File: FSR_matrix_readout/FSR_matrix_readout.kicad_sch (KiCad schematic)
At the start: 6 parts, among them U1 NCD98010XMXTAG, U2 NCD98010XMXTAG, U4 TPW4051-QF4R, U5 TPW4051-QF4R

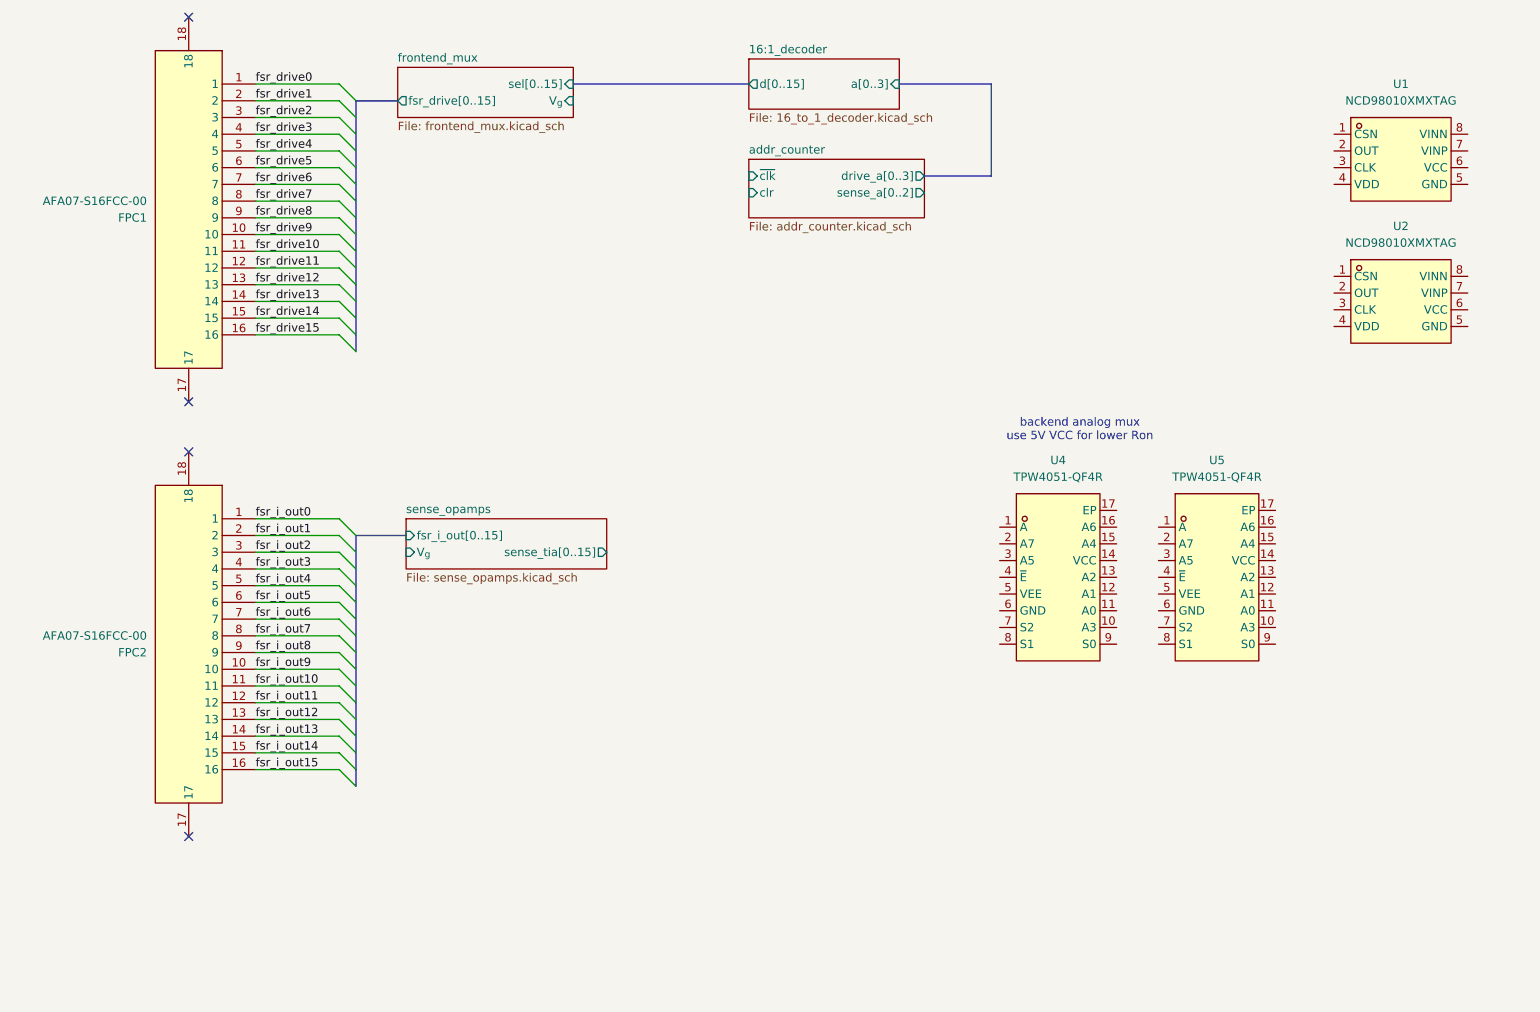
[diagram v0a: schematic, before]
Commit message: done backend_mux; cleanup connection; start dynamic gain opamp
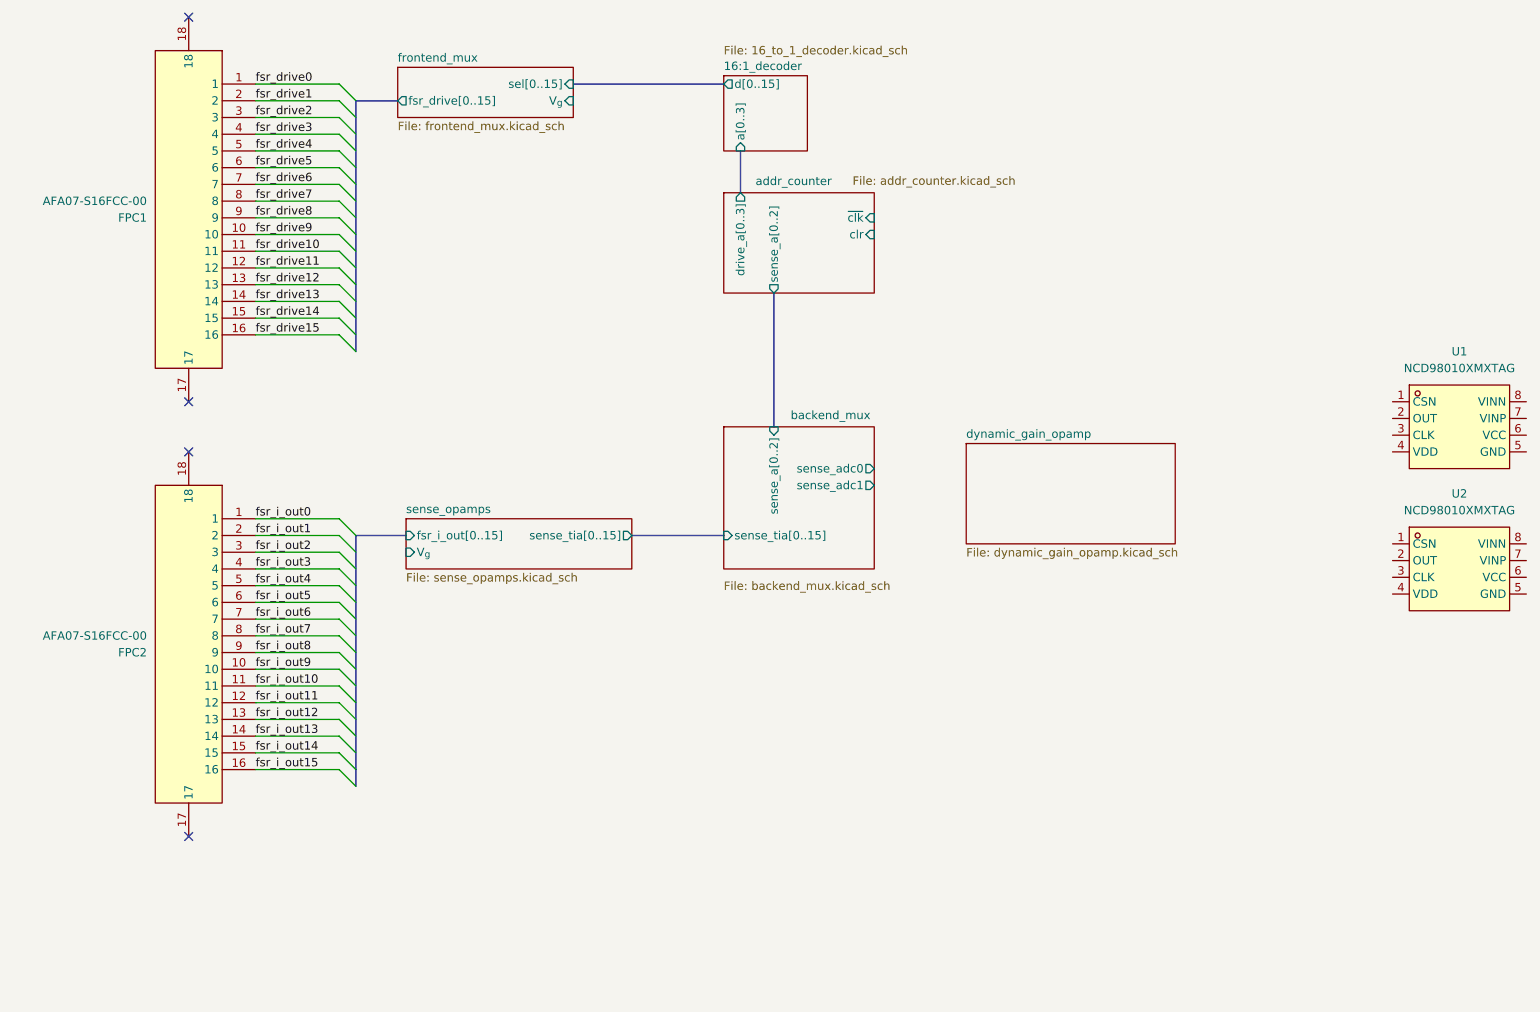
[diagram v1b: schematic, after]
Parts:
- removed U4, U5: TPW4051-QF4R, easyeda2kicad:WQFN-16_L3.0-W3.0-P0.50-TL-EP1.7, symbol lcsc:TPW4051-QF4R
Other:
- added sheet backend_mux (backend_mux.kicad_sch)
- added sheet dynamic_gain_opamp (dynamic_gain_opamp.kicad_sch)
- note removed: "backend analog mux use 5V VCC for lower Ron"
- moved on the sheet: U1, U2

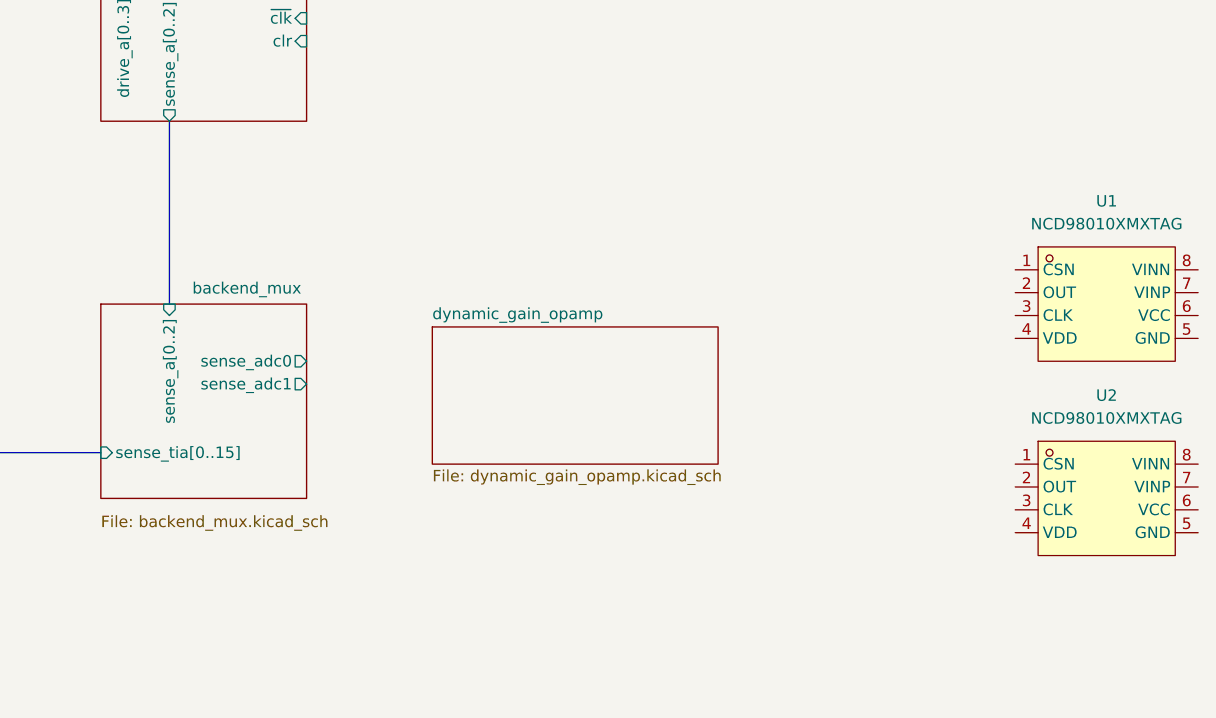
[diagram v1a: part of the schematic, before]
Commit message: done PGA and ADC
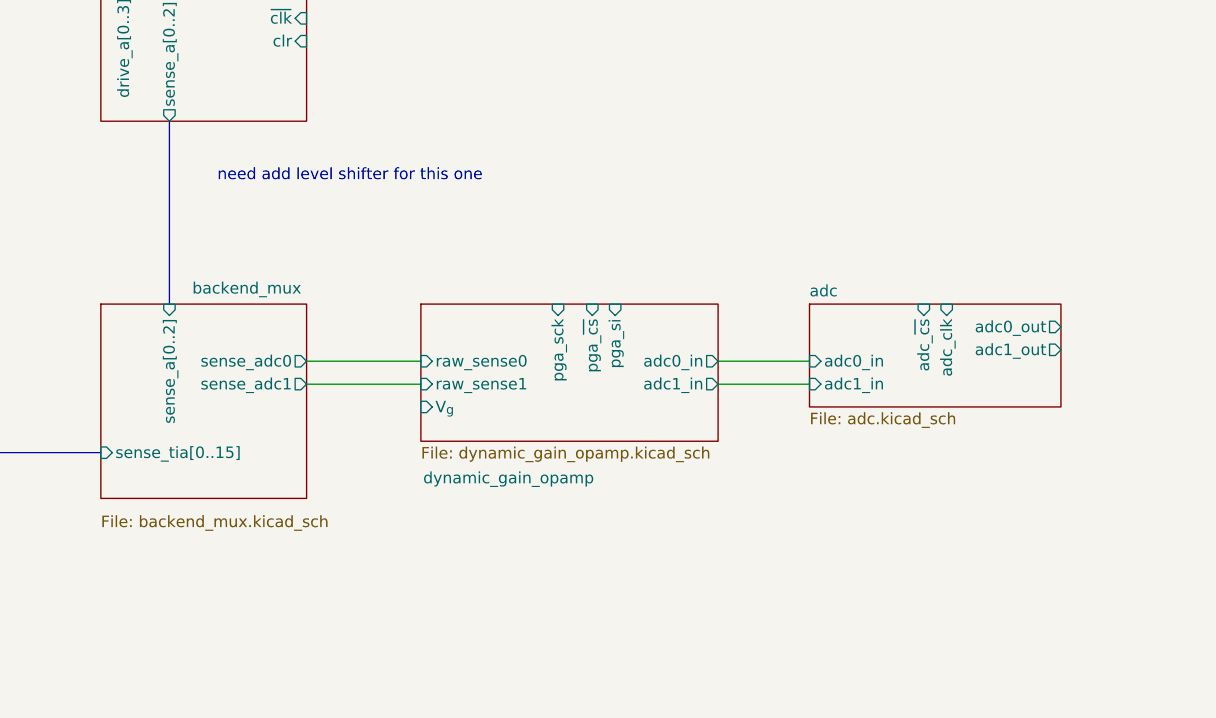
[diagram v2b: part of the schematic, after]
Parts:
- removed U1, U2: NCD98010XMXTAG, easyeda2kicad:X2QFN-8_L1.5-W1.5-P0.50-BL, symbol lcsc:NCD98010XMXTAG
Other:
- added sheet adc (adc.kicad_sch)
- sheet dynamic_gain_opamp ports: added V_{g}, adc0_in, adc1_in, pga_sck, pga_si, pga_~{cs}, raw_sense0, raw_sense1; removed none
- note added: "need add level shifter for this one"

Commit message: done everything except MCU
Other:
- added sheet power (power.kicad_sch)
- note removed: "need add level shifter for this one"
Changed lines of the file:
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@@
 	(generator_version "10.0")
 	(paper "A4")
-	(text "need add level shifter for this one"
-		(exclude_from_sim no)
-		(at 145.796 70.866 0)
-		(effects
-			(font
-				(size 1.27 1.27)
-			)
-		)
+	(junction
+		(at 90.17 67.31)
+		(diameter 0)
+		(color 0 0 0 0)
 	)
 	(no_connect
@@
 		)
 	)
+	(wire
+		(pts
+			(xy 82.55 67.31) (xy 90.17 67.31)
+		)
+		(stroke
+			(width 0)
+			(type default)
+		)
+	)
 	(bus
 		(pts
@@
 	(wire
 		(pts
+			(xy 90.17 67.31) (xy 90.17 96.52)
+		)
+		(stroke
+			(width 0)
+			(type default)
+		)
+	)
+	(wire
+		(pts
 			(xy 46.99 50.8) (xy 59.69 50.8)
 		)
@@
 		(pts
 			(xy 46.99 53.34) (xy 59.69 53.34)
+		)
+		(stroke
+			(width 0)
+			(type default)
+		)
+	)
+	(wire
+		(pts
+			(xy 90.17 38.1) (xy 90.17 67.31)
 		)
 		(stroke
@@
 		(on_board yes)
 		(dnp no)
-		(fields_autoplaced yes)
 		(stroke
 			(width 0.1524)
@@
 		)
 		(property "Sheetfile" "frontend_mux.kicad_sch"
-			(at 68.58 38.6846 0)
+			(at 68.58 26.162 0)
 			(show_name no)
 			(do_not_autoplace no)
@@
 		)
 		(pin "V_{g}" input
-			(at 95.25 35.56 0)
-			(effects
-				(font
-					(size 1.27 1.27)
-				)
-				(justify right)
+			(at 90.17 38.1 270)
+			(effects
+				(font
+					(size 1.27 1.27)
+				)
+				(justify left)
 			)
 		)
@@
 	(sheet
 		(at 118.11 85.09)
-		(size 22.86 21.59)
+		(size 22.86 19.05)
 		(exclude_from_sim no)
 		(in_bom yes)
@@
 				(path "/6dca5e5c-f676-465d-98c9-14af6047a226"
 					(page "5")
+				)
+			)
+		)
+	)
+	(sheet
+		(at 69.85 64.77)
+		(size 12.7 5.08)
+		(exclude_from_sim no)
+		(in_bom yes)
+		(on_board yes)
+		(dnp no)
+		(stroke
+			(width 0.1524)
+			(type solid)
+		)
+		(fill
+			(color 0 0 0 0)
+		)
+		(property "Sheetname" "power"
+			(at 69.85 64.0584 0)
+			(show_name no)
+			(do_not_autoplace no)
+			(effects
+				(font
+					(size 1.27 1.27)
+				)
+				(justify left bottom)
+			)
+		)
+		(property "Sheetfile" "power.kicad_sch"
+			(at 67.31 72.39 0)
+			(show_name no)
+			(do_not_autoplace no)
+			(effects
+				(font
+					(size 1.27 1.27)
+				)
+				(justify left top)
+			)
+		)
+		(pin "V_{g}" output
+			(at 82.55 67.31 0)
+			(effects
+				(font
+					(size 1.27 1.27)
+				)
+				(justify right)
+			)
+		)
+		(instances
+			(project "FSR_matrix_readout"
+				(path "/6dca5e5c-f676-465d-98c9-14af6047a226"
+					(page "9")
 				)
 			)
@@
 	)
 	(sheet
-		(at 69.85 99.06)
+		(at 69.85 96.52)
 		(size 34.29 7.62)
 		(exclude_from_sim no)
@@
 		)
 		(property "Sheetname" "sense_opamps"
-			(at 69.85 98.3484 0)
+			(at 69.85 95.8084 0)
 			(show_name no)
 			(do_not_autoplace no)
@@
 		)
 		(property "Sheetfile" "sense_opamps.kicad_sch"
-			(at 69.85 107.2646 0)
+			(at 69.85 104.7246 0)
 			(show_name no)
 			(do_not_autoplace no)
@@
 		)
 		(pin "V_{g}" input
-			(at 69.85 104.14 180)
-			(effects
-				(font
-					(size 1.27 1.27)
-				)
-				(justify left)
-			)
-		)
+			(at 90.17 96.52 90)
+			(effects
+				(font
+					(size 1.27 1.27)
+				)
+				(justify right)
+			)
+		)

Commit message: fix Vg-related issuies
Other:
- note added: "TODO: add bulk cap for power"
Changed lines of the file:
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@@
 	(generator_version "10.0")
 	(paper "A4")
+	(text "TODO: add bulk cap for power"
+		(exclude_from_sim no)
+		(at 189.23 33.782 0)
+		(effects
+			(font
+				(size 1.27 1.27)
+			)
+		)
+	)
+	(junction
+		(at 90.17 77.47)
+		(diameter 0)
+		(color 0 0 0 0)
+	)
 	(junction
 		(at 90.17 67.31)
@@
 	(wire
 		(pts
-			(xy 90.17 67.31) (xy 90.17 96.52)
+			(xy 90.17 67.31) (xy 90.17 77.47)
 		)
 		(stroke
@@
 	(wire
 		(pts
+			(xy 90.17 77.47) (xy 90.17 96.52)
+		)
+		(stroke
+			(width 0)
+			(type default)
+		)
+	)
+	(wire
+		(pts
 			(xy 46.99 38.1) (xy 59.69 38.1)
 		)
@@
 		(pts
 			(xy 140.97 93.98) (xy 153.67 93.98)
+		)
+		(stroke
+			(width 0)
+			(type default)
+		)
+	)
+	(wire
+		(pts
+			(xy 157.48 77.47) (xy 157.48 85.09)
+		)
+		(stroke
+			(width 0)
+			(type default)
+		)
+	)
+	(wire
+		(pts
+			(xy 90.17 77.47) (xy 157.48 77.47)
 		)
 		(stroke
@@
 		)
 		(pin "V_{g}" input
-			(at 153.67 96.52 180)
-			(effects
-				(font
-					(size 1.27 1.27)
-				)
-				(justify left)
-			)
-		)
+			(at 157.48 85.09 90)
+			(effects
+				(font
+					(size 1.27 1.27)
+				)
+				(justify right)
+			)
+		)

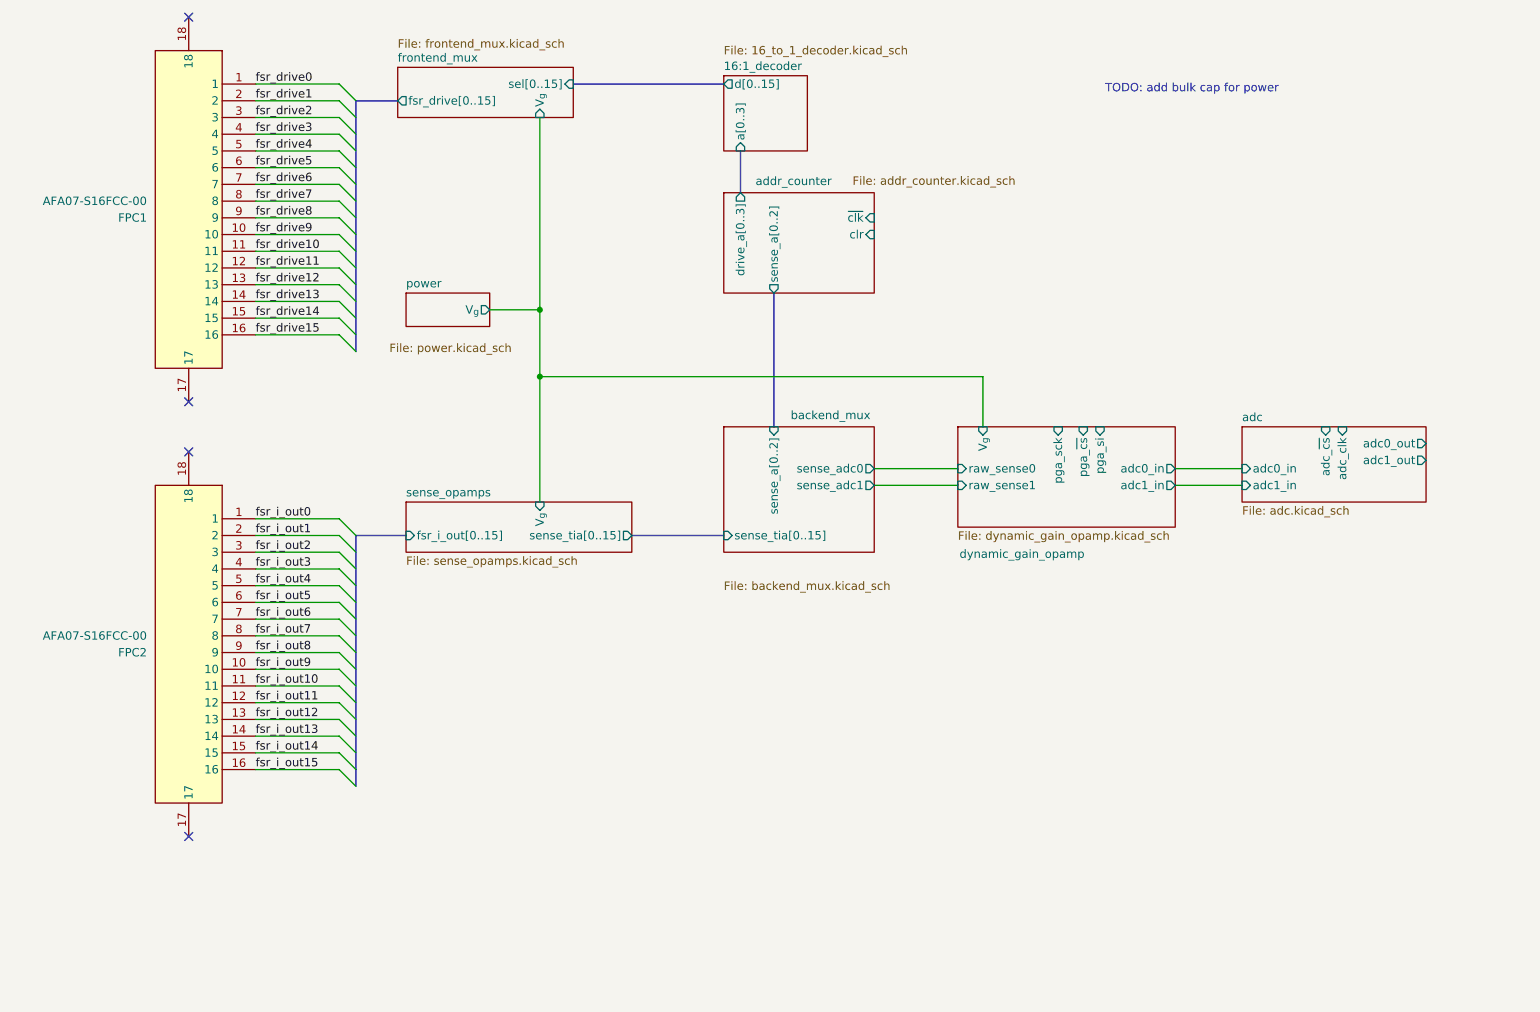
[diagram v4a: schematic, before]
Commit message: add esp devboard module and finished connection
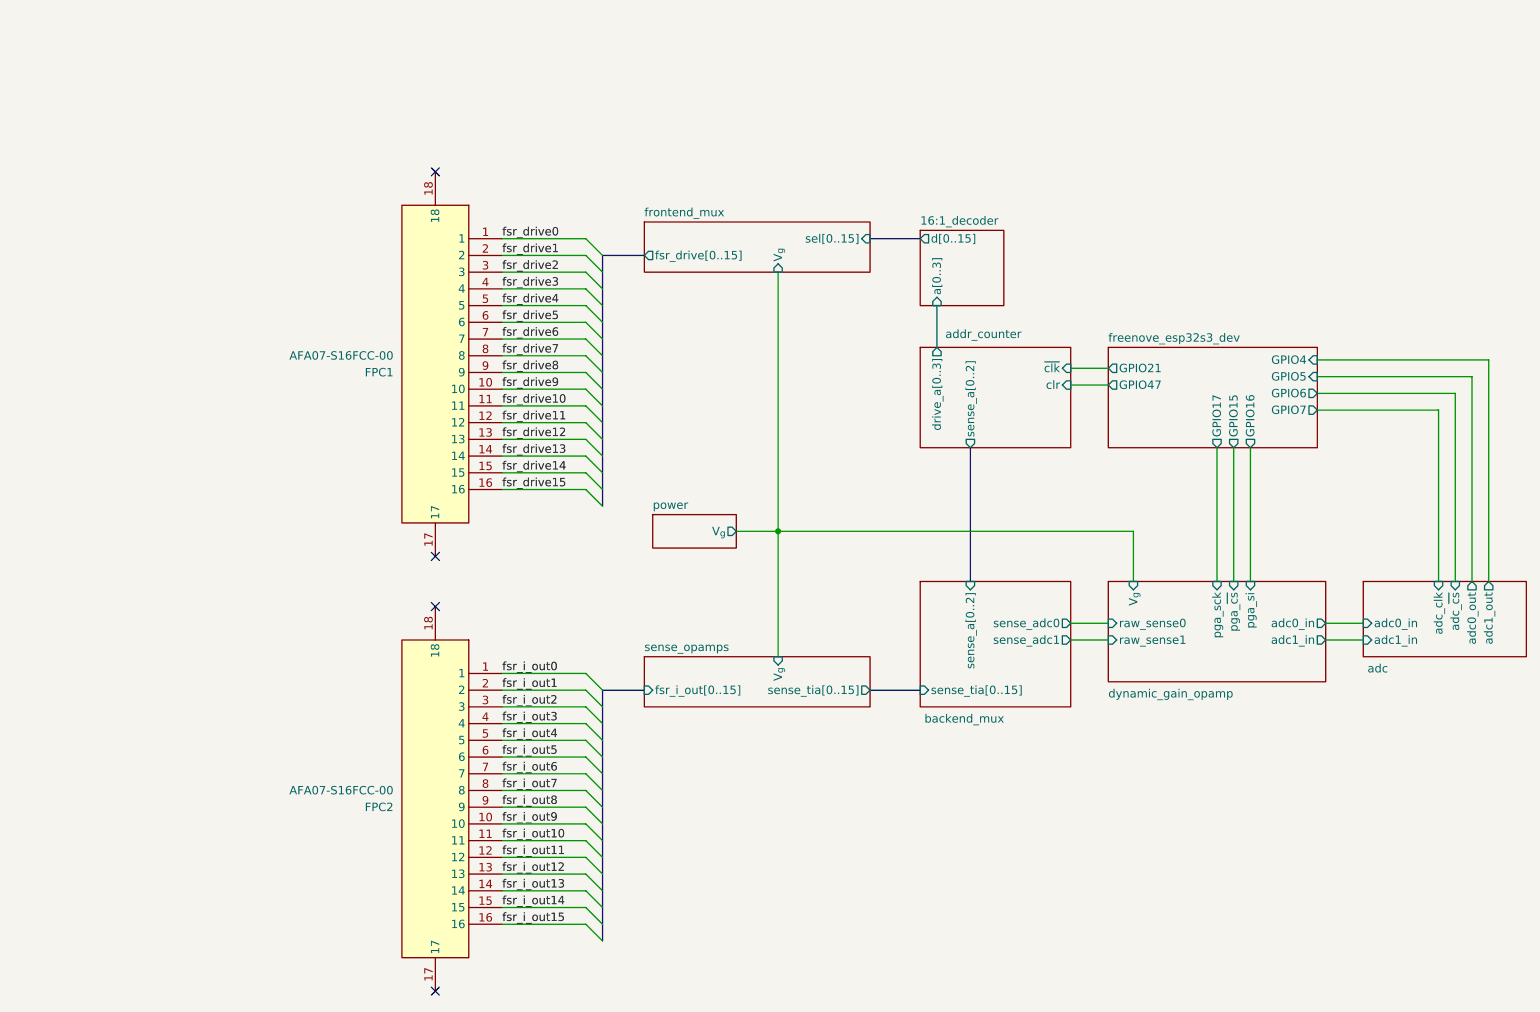
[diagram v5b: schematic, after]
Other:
- added sheet freenove_esp32s3_dev (freenove_esp32s3_dev.kicad_sch)
- note removed: "TODO: add bulk cap for power"
- moved on the sheet: FPC1, FPC2
